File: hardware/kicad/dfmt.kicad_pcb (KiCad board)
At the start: 2 copper layers, 50 x 50 mm, 38 parts, among them IC1 SI4735-D60, IC2 SI4735-D60, IC3 LE33-SMT, P1 FM ANT, P2 AM ANT, P3 PROG, P4 USB_OTG, SW1 UP, SW2 DOWN, Y1 8MHz

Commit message: PCB second try. Unfinished
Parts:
- C10, C12, C13, C16, C4, C5, C8, C9, IC2, IC3, L1, R7, Y1: moved to B.Cu
- C2, C3, C7, IC1, R8, R9: moved to F.Cu
- R1: value 600R -> 5R6; moved to F.Cu
- R2, R3: value 2k -> 2k2; moved to F.Cu
- R4: value 600R -> 5R6; moved to B.Cu
- R5, R6: value 2k -> 2k2; moved to B.Cu
- moved P2 66.8 mm to (227.8, 29.2)
- moved P1 62.9 mm to (227.6, 59.9), turned to 180 degrees
- moved R4 61.2 mm to (240.2, 40.5), turned to 270 degrees
- moved R5 57.5 mm to (237.2, 40.5), turned to 270 degrees
- moved C1 56.3 mm to (227.6, 65.8), turned to 90 degrees
- moved R6 53.9 mm to (234.2, 40.5), turned to 270 degrees
- moved C4 51.0 mm to (231.2, 40.5), turned to 90 degrees
- moved C5 47.7 mm to (228.2, 40.5), turned to 90 degrees
- moved IC2 45.0 mm to (234.7, 31.0), turned to 90 degrees
- moved C8 38.9 mm to (234.9, 23.9), turned to 180 degrees
- moved C9 33.8 mm to (228.1, 23.6), turned to 90 degrees
- moved R8 32.9 mm to (267.0, 82.8), turned to 0 degrees
- moved R9 25.1 mm to (267.0, 78.0), turned to 0 degrees
- moved C16 17.5 mm to (258.6, 29.7)
- moved R2 16.9 mm to (237.2, 49.5)
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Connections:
- net Net-(MCU1-Pad12) renamed /DOUT_B
- net Net-(MCU1-Pad14) renamed /DOUT_A
- MCU1 pad 25: Net-(MCU1-Pad25) -> /DCLK
- MCU1 pad 26: Net-(MCU1-Pad26) -> /DCLK
- MCU1 pad 4: Net-(MCU1-Pad4) -> /DFS
- MCU1 pad 7: Net-(MCU1-Pad7) -> /DFS
- P3 pad 2: Net-(MCU1-Pad4) -> /DFS
- P4 pad 6: Net-(P4-Pad6) -> GND
- R2 pad 2: Net-(MCU1-Pad7) -> /DFS
- R3 pad 2: Net-(MCU1-Pad25) -> /DCLK
- R5 pad 2: Net-(MCU1-Pad4) -> /DFS
- R6 pad 2: Net-(MCU1-Pad26) -> /DCLK
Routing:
- net /RST: track 0.00 -> 72.0 mm, vias 0 -> 1
- net GND: track 123.2 -> 179.5 mm
- net /DCLK: track 0.00 -> 45.6 mm, vias 0 -> 2
- net /SDA: track 44.1 -> 0.00 mm
- net /DFS: track 0.00 -> 32.8 mm, vias 0 -> 1
- net VDD: track 67.8 -> 91.6 mm, vias 0 -> 2
- net /DOUT_B: track 0.00 -> 20.7 mm, vias 0 -> 1
- net Net-(P4-Pad6): track 19.9 -> 0.00 mm
- net Net-(C2-Pad1): track 0.00 -> 18.8 mm, vias 0 -> 1
- net Net-(C3-Pad1): track 0.00 -> 18.4 mm, vias 0 -> 1
- net Net-(MCU1-Pad24): track 21.6 -> 34.8 mm, vias 0 -> 1
- net Net-(MCU1-Pad16): track 29.6 -> 17.0 mm
- net Net-(MCU1-Pad21): track 10.1 -> 0.00 mm
- net Net-(MCU1-Pad22): track 10.1 -> 0.00 mm
- net Net-(C11-Pad1): track 14.2 -> 5.04 mm
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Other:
- outline, holes or cut-outs redrawn
- net class Default: trace_width 0.25 -> 0.3; via_dia 0.6 -> 0.7; via_drill 0.4 -> 0.5
- net class Power added: clearance 0.5, trace_width 1, via_dia 1, via_drill 0.8
- net class pwr removed

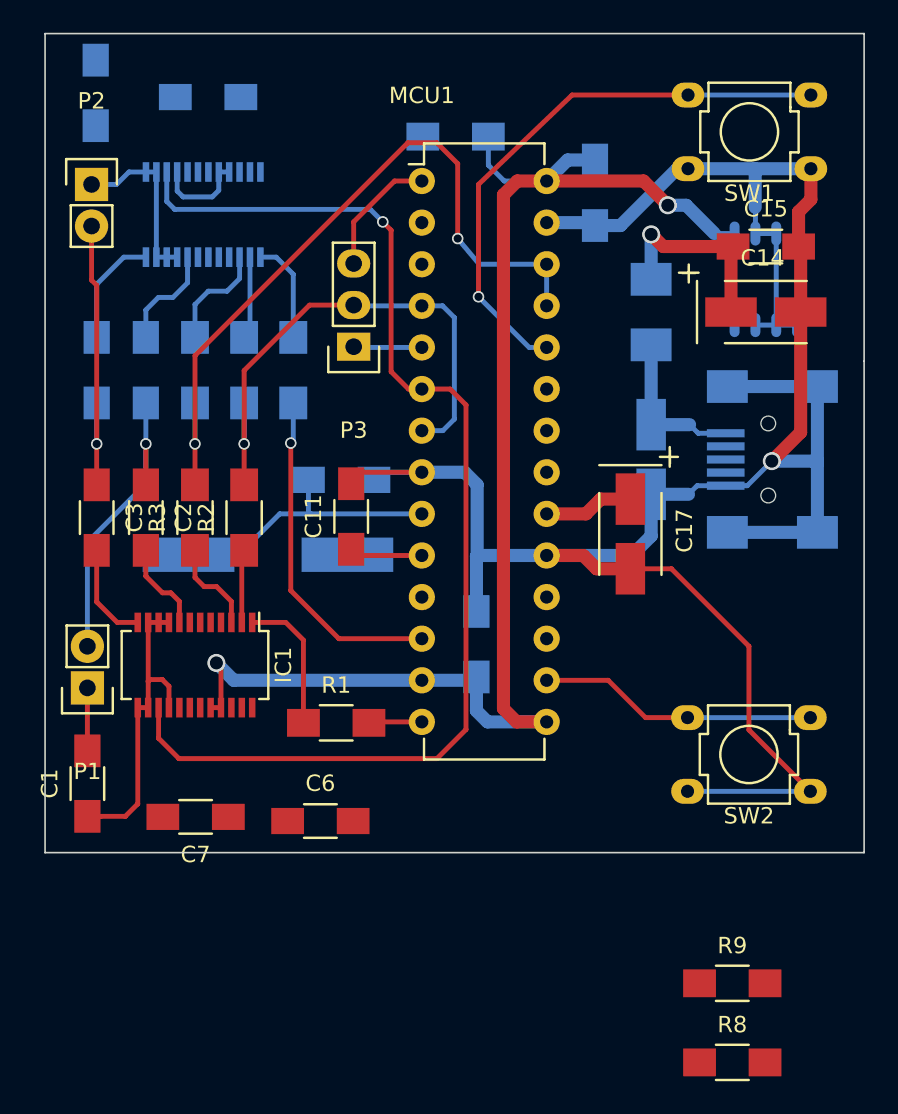
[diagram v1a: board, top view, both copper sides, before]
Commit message: Borad v 1.0 without logo. Verification of USB connector needed ! There are no holes but place on edges.
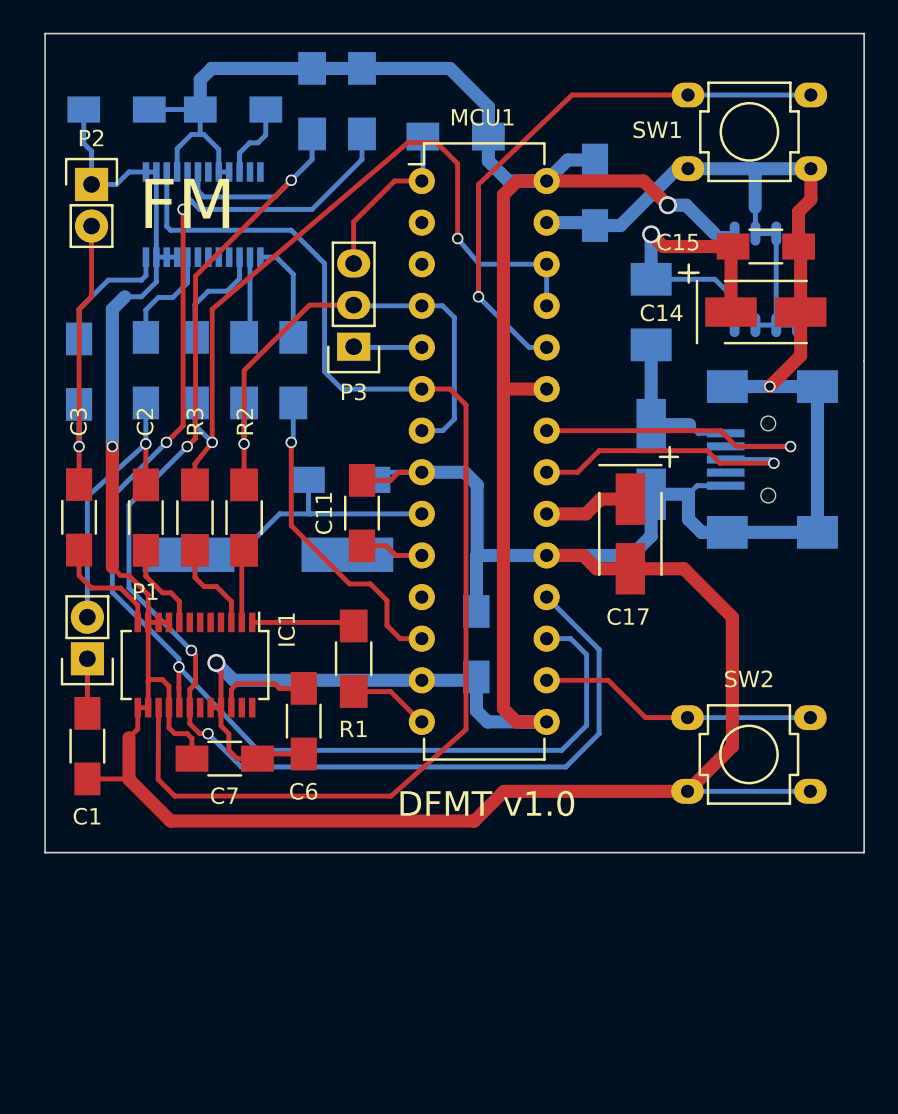
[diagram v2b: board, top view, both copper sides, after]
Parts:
- R8, R9: moved to B.Cu
- moved R8 64.0 mm to (241.3, 24.1), turned to 270 degrees
- moved R9 58.4 mm to (244.3, 24.1), turned to 270 degrees
- moved C6 6.18 mm to (240.8, 62.0), turned to 270 degrees
- moved R1 4.05 mm to (243.8, 58.2), turned to 270 degrees
- moved C7 3.98 mm to (236.0, 64.3)
- moved C1 2.29 mm to (227.6, 63.5)
- moved P1 1.78 mm to (227.6, 58.2)
- moved C8 1.70 mm to (236.5, 24.6)
- moved C9 1.63 mm to (229.4, 24.6), turned to 180 degrees
- moved C5 1.08 mm to (227.1, 40.6)
- moved C3 1.08 mm to (227.1, 49.5)
- moved C11 0.69 mm to (244.3, 49.3)
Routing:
- net /SDA: track 0.00 -> 86.5 mm, vias 0 -> 4
- net /SCLK: track 0.00 -> 84.8 mm, vias 0 -> 3
- net GND: track 179.5 -> 238.7 mm, vias 1 -> 2
- net VDD: track 91.6 -> 130.2 mm
- net Net-(MCU1-Pad22): track 0.00 -> 19.3 mm, vias 0 -> 1
- net Net-(MCU1-Pad21): track 0.00 -> 17.8 mm, vias 0 -> 1
- net Net-(C14-Pad1): track 12.3 -> 19.5 mm
- net Net-(C6-Pad1): track 0.00 -> 5.79 mm
- net Net-(C8-Pad1): track 0.00 -> 4.77 mm
- net Net-(C11-Pad1): track 5.04 -> 8.55 mm
- net /RST: track 72.0 -> 74.9 mm, vias 1 -> 0
- net Net-(MCU1-Pad1): track 7.73 -> 10.5 mm
- net Net-(IC1-Pad1): track 8.62 -> 6.29 mm
- net /DOUT_A: track 3.25 -> 4.93 mm
- net Net-(C2-Pad1): track 18.8 -> 17.2 mm
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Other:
- board text added: "AM"
- board text added: "DFMT v1.0"
- board text added: "FM"
